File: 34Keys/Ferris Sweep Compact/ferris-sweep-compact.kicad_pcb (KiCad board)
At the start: 2 copper layers, 107.5 x 86.7 mm, 21 parts, among them J1 MJ-4PP-9, SW10 SW_PUSH, SW11 SW_PUSH, SW12 SW_PUSH, SW14 SW_PUSH, SW15 SW_PUSH, SW16 SW_PUSH, SW17 SW_PUSH, SW18 SW_PUSH, SW2 SW_PUSH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

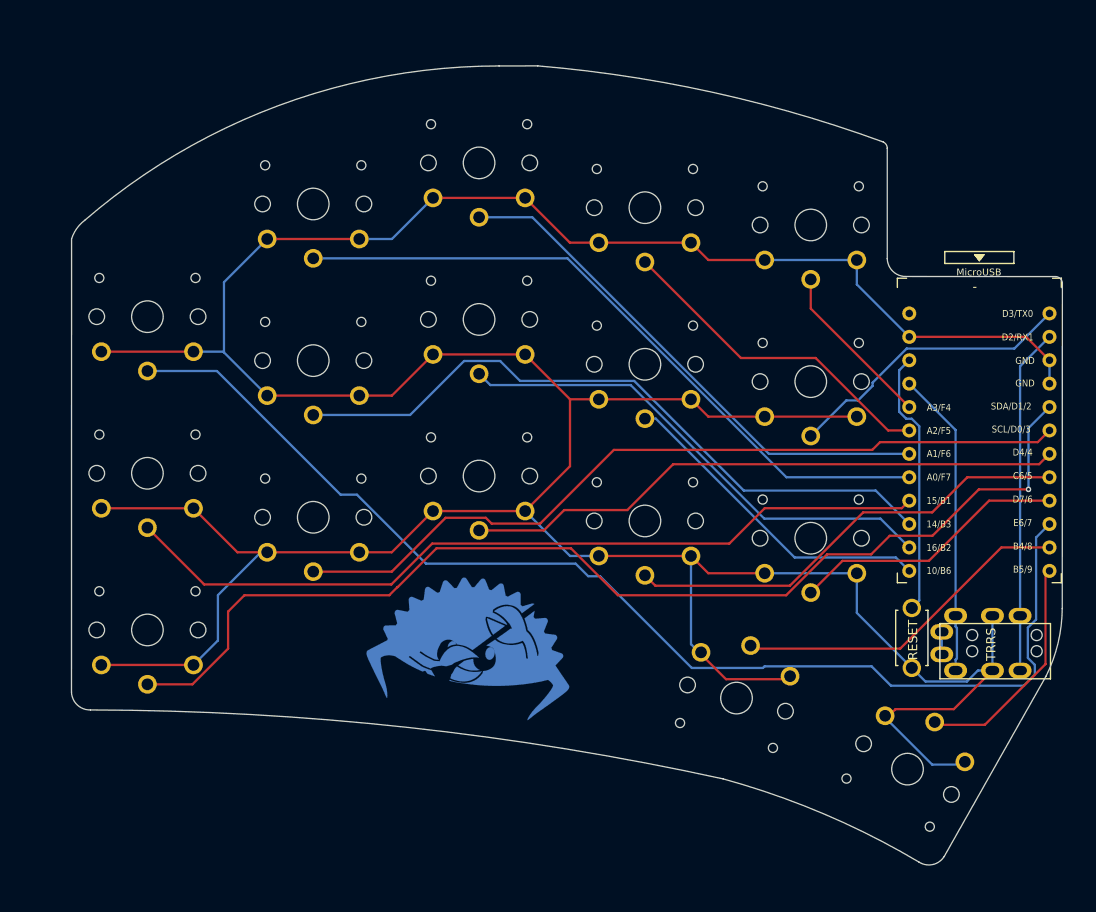
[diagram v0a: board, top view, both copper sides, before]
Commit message: manual routing for ferris sweep.
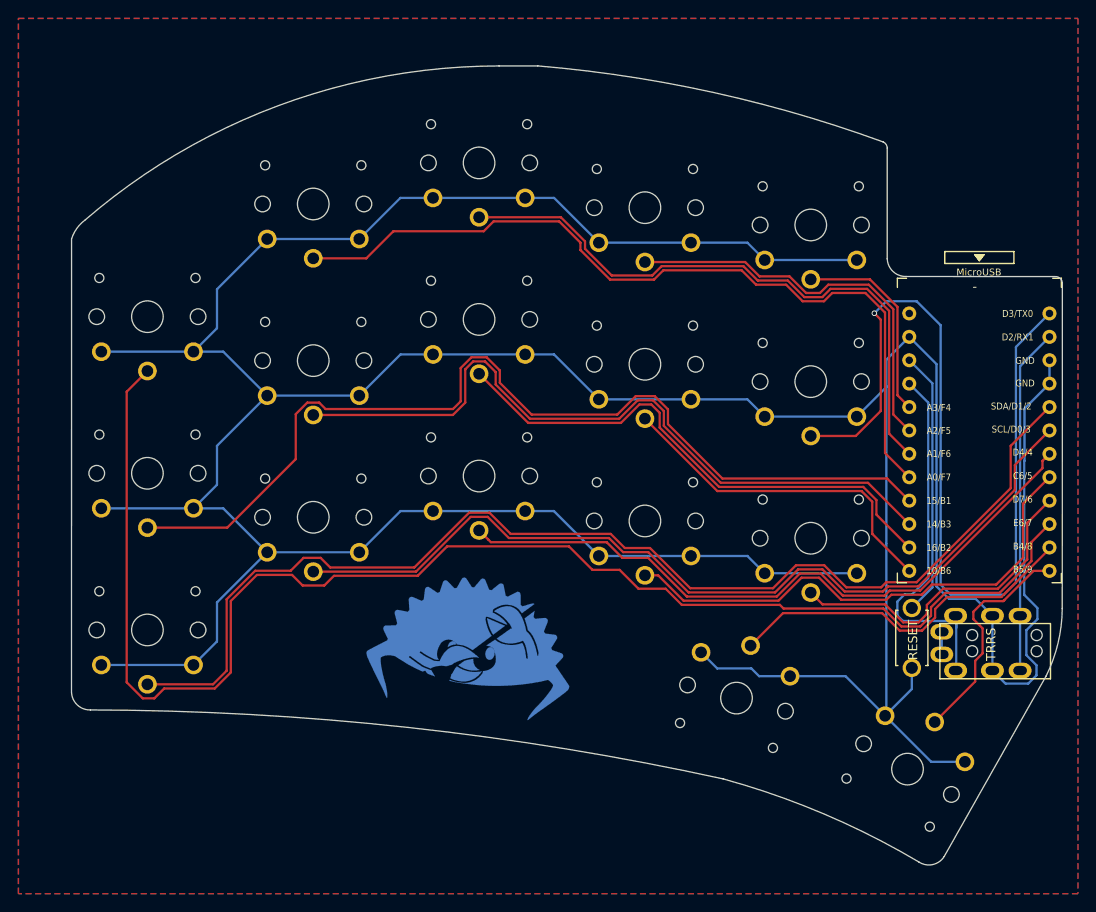
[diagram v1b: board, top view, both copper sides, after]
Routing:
- net GND: track 404.7 -> 473.7 mm
- net LED: track 31.6 -> 96.5 mm, vias 0 -> 1
- net row3: track 128.8 -> 157.9 mm
- net col4: track 89.0 -> 105.7 mm
- net col3: track 74.5 -> 88.8 mm
- net col2: track 57.3 -> 67.2 mm
- net SCL: track 86.8 -> 96.6 mm
- net VCC: track 33.3 -> 41.9 mm
- net row0: track 65.4 -> 73.8 mm
- net col1: track 36.3 -> 43.7 mm
- net row1: track 49.3 -> 56.0 mm
- net SDA: track 120.9 -> 127.3 mm, vias 1 -> 0
- net row2: track 30.0 -> 35.6 mm
- net col5: track 74.4 -> 79.9 mm
- net col0: track 18.3 -> 22.1 mm
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- added copper zone on B.Cu, net (none)
- added copper zone on F.Cu, net (none)

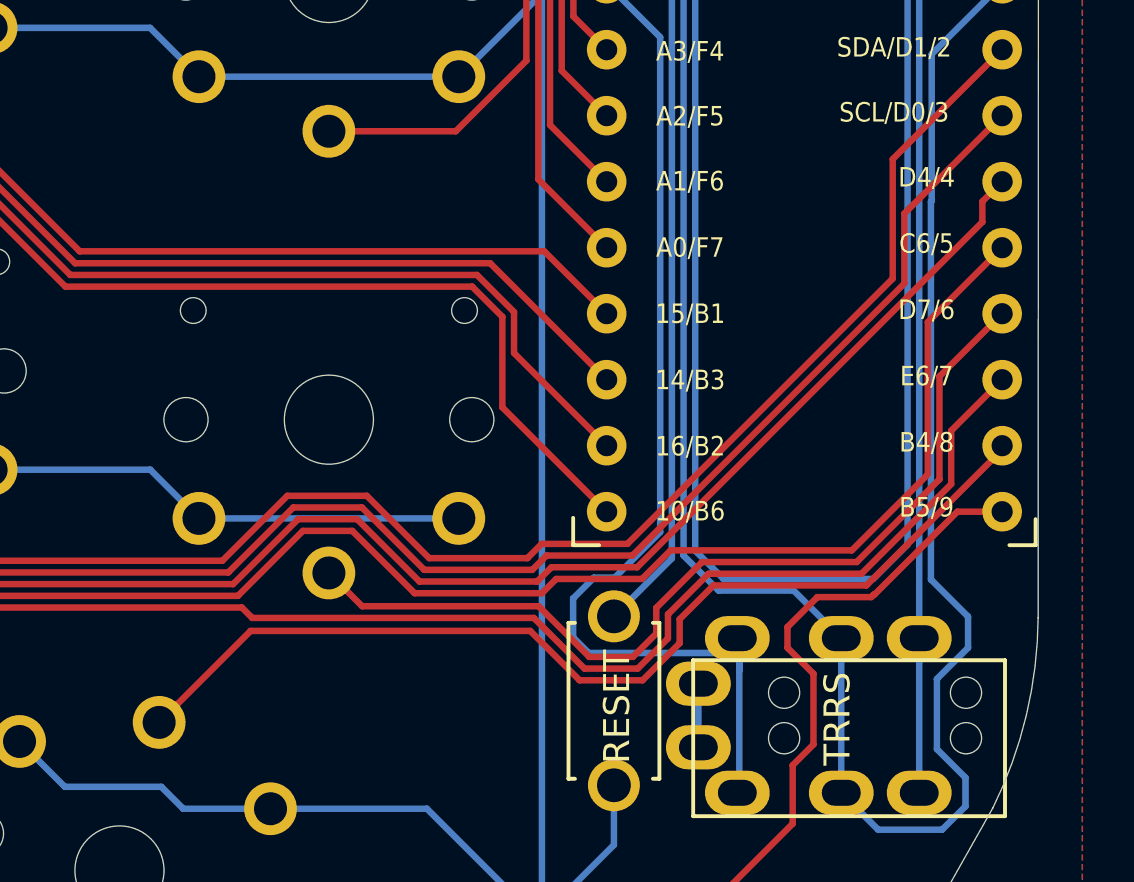
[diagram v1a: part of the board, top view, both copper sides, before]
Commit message: fixed some wilding tracks.
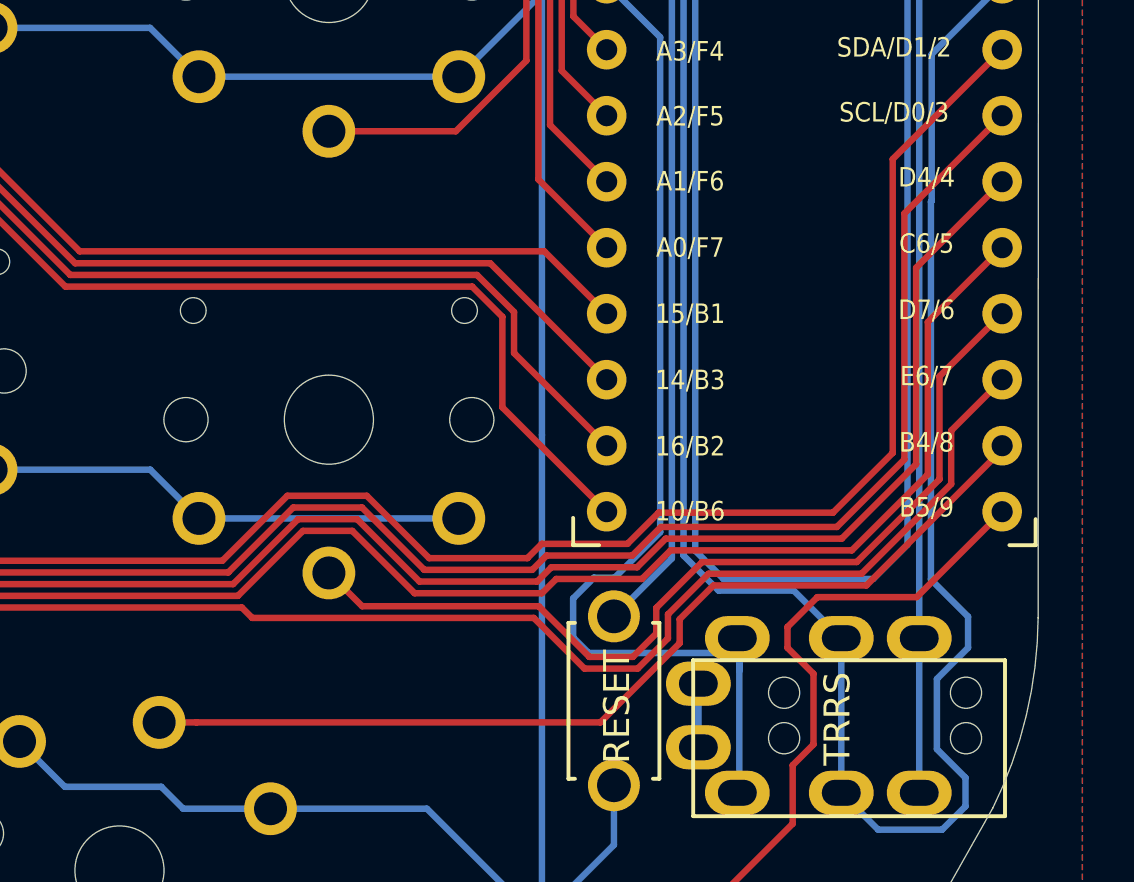
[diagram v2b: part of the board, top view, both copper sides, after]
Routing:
- net SCL: track 96.6 -> 100.6 mm
- net row0: track 73.8 -> 77.7 mm
- net SDA: track 127.3 -> 131.2 mm
- net Net-(U1-Pad11): track 39.1 -> 37.5 mm
